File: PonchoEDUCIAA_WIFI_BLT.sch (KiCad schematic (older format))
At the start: 24 parts, among them J1 UART, SW1 Reset, SW2 Boot, U1 ESP32-WROOM

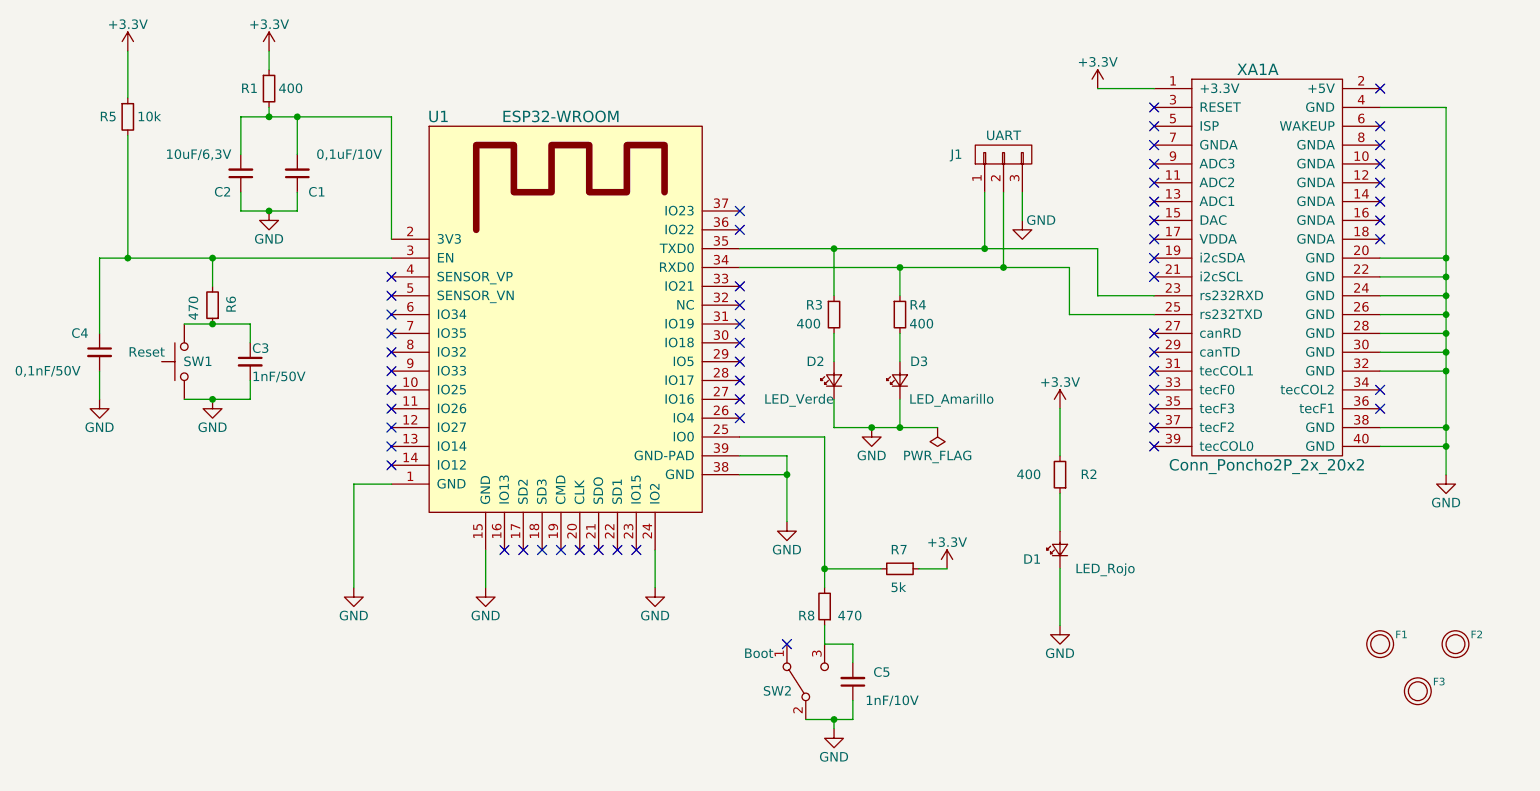
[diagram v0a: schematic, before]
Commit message: Se cargan todos los campos de los componentes del esquematico y se exporta el bom y se generan documentos
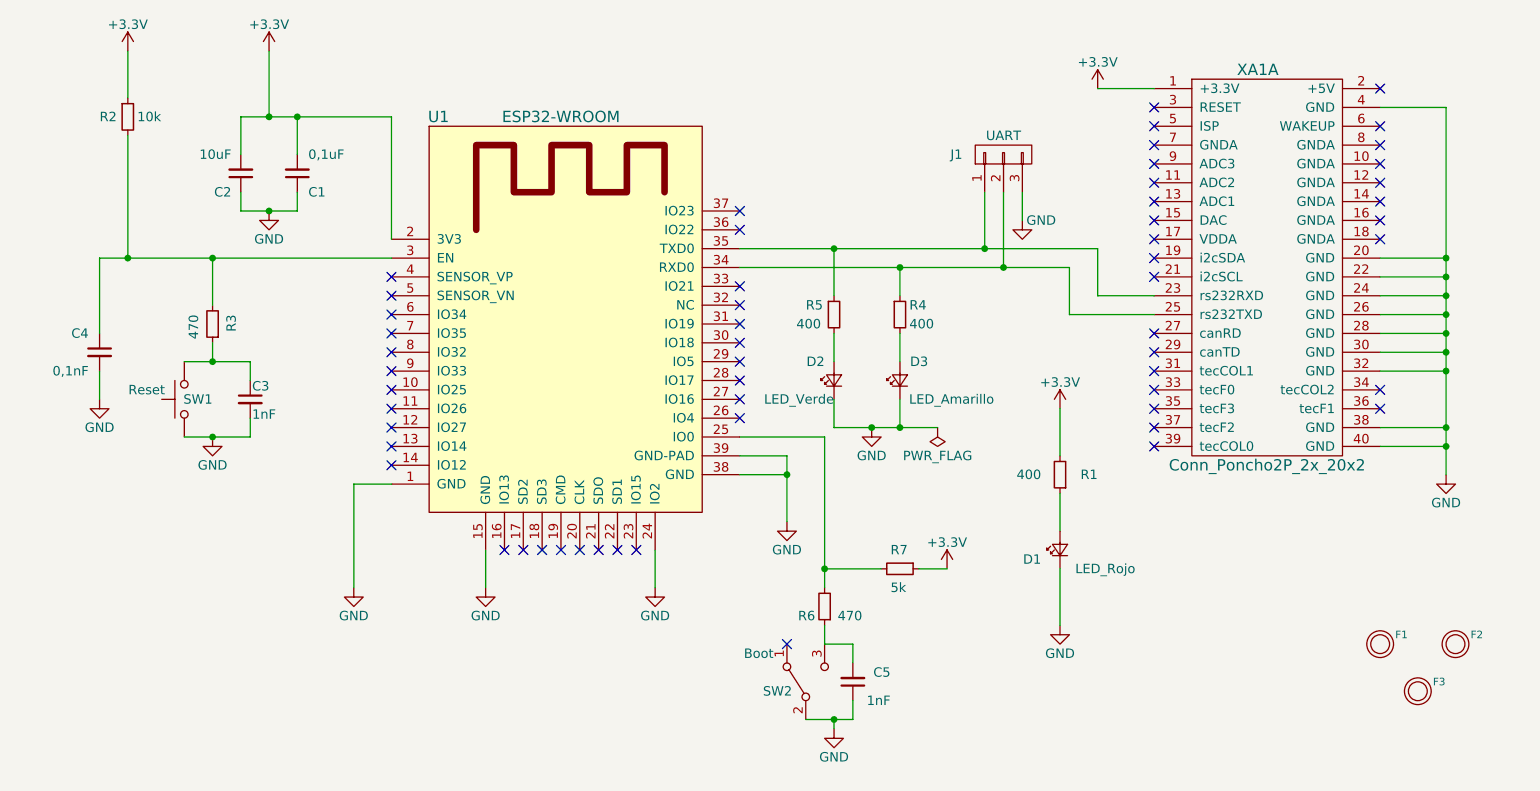
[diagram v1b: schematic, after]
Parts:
- removed R1: 400, Resistors_SMD:R_1206_HandSoldering, symbol R_Small
- C1: value 0,1uF/10V -> 0,1uF
- C2: value 10uF/6,3V -> 10uF
- C3: value 1nF/50V -> 1nF
- C4: value 0,1nF/50V -> 0,1nF
- C5: value 1nF/10V -> 1nF
- D1: Desc (none) -> LED 5MM 5V VERTICAL RED PC MNT; Digikey# (none) -> 350-1608-ND; Manf (none) -> Dialight; Manf# (none) -> 5500504F
- D2: Desc (none) -> LED 5MM VERT HE DIFF GRN PC MNT; Digikey# (none) -> 350-2814-ND; Manf (none) -> Dialight; Manf# (none) -> 5612201050F
- D3: Desc (none) -> LED 5MM 5V VERTICAL YELLOW PCMNT; Digikey# (none) -> 350-1615-ND; Manf (none) -> Dialight; Manf# (none) -> 5500804F
- J1: Desc (none) -> CONN HEADER 3POS .100 VERT TIN; Digikey# (none) -> WM4112-ND; Manf (none) -> Molex, LLC; Manf# (none) -> 0022272031
- R1: renamed from R2; Desc (none) -> RES SMD 400 OHM 0.1% 0.15W 0603; Digikey# (none) -> PAT400ACT-ND; Manf (none) -> Vishay Thin Film; Manf# (none) -> PAT0603E4000BST1
- R3: renamed from R6; Desc (none) -> RES SMD 470 OHM 1% 1/16W 0402; Digikey# (none) -> RMCF0402FT470RCT-ND; Manf (none) -> Stackpole Electronics Inc.; Manf# (none) -> RMCF0402FT470R
- R4: Desc (none) -> RES SMD 400 OHM 0.1% 0.15W 0603; Digikey# (none) -> PAT400ACT-ND; Manf (none) -> Vishay Thin Film; Manf# (none) -> PAT0603E4000BST1
- R5: renamed from R3; Desc (none) -> RES SMD 400 OHM 0.1% 0.15W 0603; Digikey# (none) -> PAT400ACT-ND; Manf (none) -> Vishay Thin Film; Manf# (none) -> PAT0603E4000BST1
- R6: renamed from R8; Desc (none) -> RES SMD 470 OHM 1% 1/16W 0402; Digikey# (none) -> RMCF0402FT470RCT-ND; Manf (none) -> Stackpole Electronics Inc.; Manf# (none) -> RMCF0402FT470R
- R7: Desc (none) -> RES SMD 5K OHM 0.05% 1/4W 1206; Digikey# (none) -> 541-3307-1-ND; Manf (none) -> Vishay Dale; Manf# (none) -> TNPU12065K00AZEN00
- SW1: Desc (none) -> SWITCH PUSH SPST-NO 0.1A 32V; Digikey# (none) -> 401-1969-ND; Manf (none) -> C&K; Manf# (none) -> D6C90 F1 LFS
- SW2: Desc (none) -> SWITCH SLIDE DPDT 300MA 6V; Digikey# (none) -> 401-2001-ND; Manf (none) -> C&K; Manf# (none) -> JS202011CQN
- U1: Desc (none) -> TXRX MOD BLE WIFI ESP-WROOM-32; Digikey# (none) -> 1528-1801-ND; Manf (none) -> Adafruit Industries LLC; Manf# (none) -> 3320
- XA1: Desc (none) -> CONN HDR 1.27MM VERT AU 20POS; Digikey# (none) -> 952-1386-ND; Manf (none) -> Harwin Inc.; Manf# (none) -> M50-3501042
- renumbered R5 to R2
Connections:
- net +3V3: now also C1.2, C2.2, U1.2 (3V3)
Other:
- moved on the sheet: C3, R3, SW1

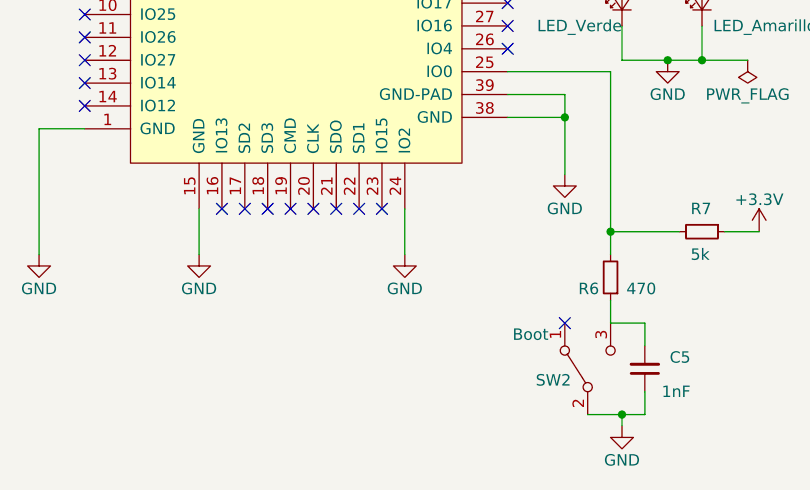
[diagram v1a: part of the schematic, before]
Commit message: Se agrega resistencia sugerida por revisor
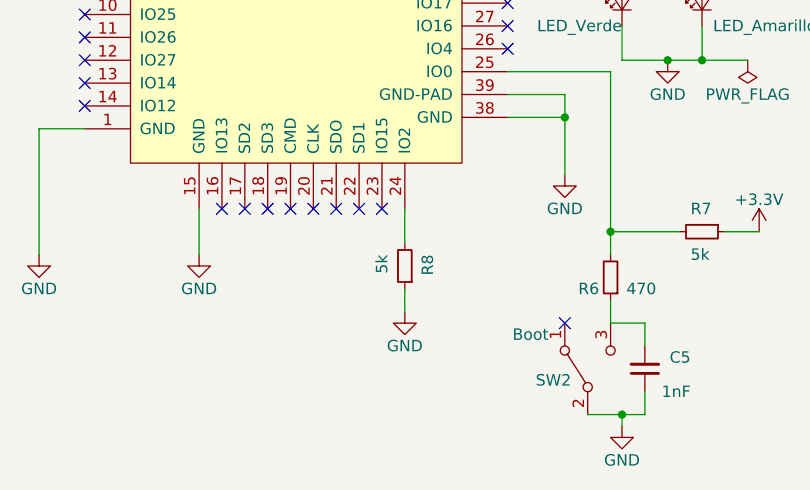
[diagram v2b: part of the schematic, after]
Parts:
- added R8: 5k, Resistors_SMD:R_1206_HandSoldering, symbol R_Small
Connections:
- net GND: now also R8.1; no longer U1.24 (IO2)
- new net: R8.2, U1.24 (IO2)
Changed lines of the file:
@@
 L GND #PWR015
 U 1 1 592E9A6D
-P 5350 5250
-F 0 "#PWR015" H 5350 5000 50  0001 C CNN
-F 1 "GND" H 5350 5100 50  0000 C CNN
-F 2 "" H 5350 5250 50  0001 C CNN
-F 3 "" H 5350 5250 50  0001 C CNN
-	1    5350 5250
+P 5350 5500
+F 0 "#PWR015" H 5350 5250 50  0001 C CNN
+F 1 "GND" H 5350 5350 50  0000 C CNN
+F 2 "" H 5350 5500 50  0001 C CNN
+F 3 "" H 5350 5500 50  0001 C CNN
+	1    5350 5500
 	1    0    0    -1
 $EndComp
@@
 Wire Wire Line
 	4450 5050 4450 5250
-Wire Wire Line
-	5350 5050 5350 5250
 Wire Wire Line
 	6300 3450 6300 3700
@@
 Wire Wire Line
 	3000 3950 3000 4050
+$Comp
+L R_Small R8
+U 1 1 594ED4F2
+P 5350 5300
+F 0 "R8" V 5250 5250 50  0000 L CNN
+F 1 "5k" V 5450 5250 50  0000 L CNN
+F 2 "Resistors_SMD:R_1206_HandSoldering" H 5350 5300 50  0001 C CNN
+F 3 "http://www.vishay.com/docs/28779/tnpue3.pdf" H 5350 5300 50  0001 C CNN
+F 4 "Vishay Dale" H 5350 5300 60  0001 C CNN "Manf"
+F 5 "TNPU12065K00AZEN00" H 5350 5300 60  0001 C CNN "Manf#"
+F 6 "541-3307-1-ND" H 5350 5300 60  0001 C CNN "Digikey#"
+F 7 "RES SMD 5K OHM 0.05% 1/4W 1206" H 5350 5300 60  0001 C CNN "Desc"
+	1    5350 5300
+	-1   0    0    1
+$EndComp
+Wire Wire Line
+	5350 5050 5350 5200
+Wire Wire Line
+	5350 5400 5350 5500
 $EndSCHEMATC

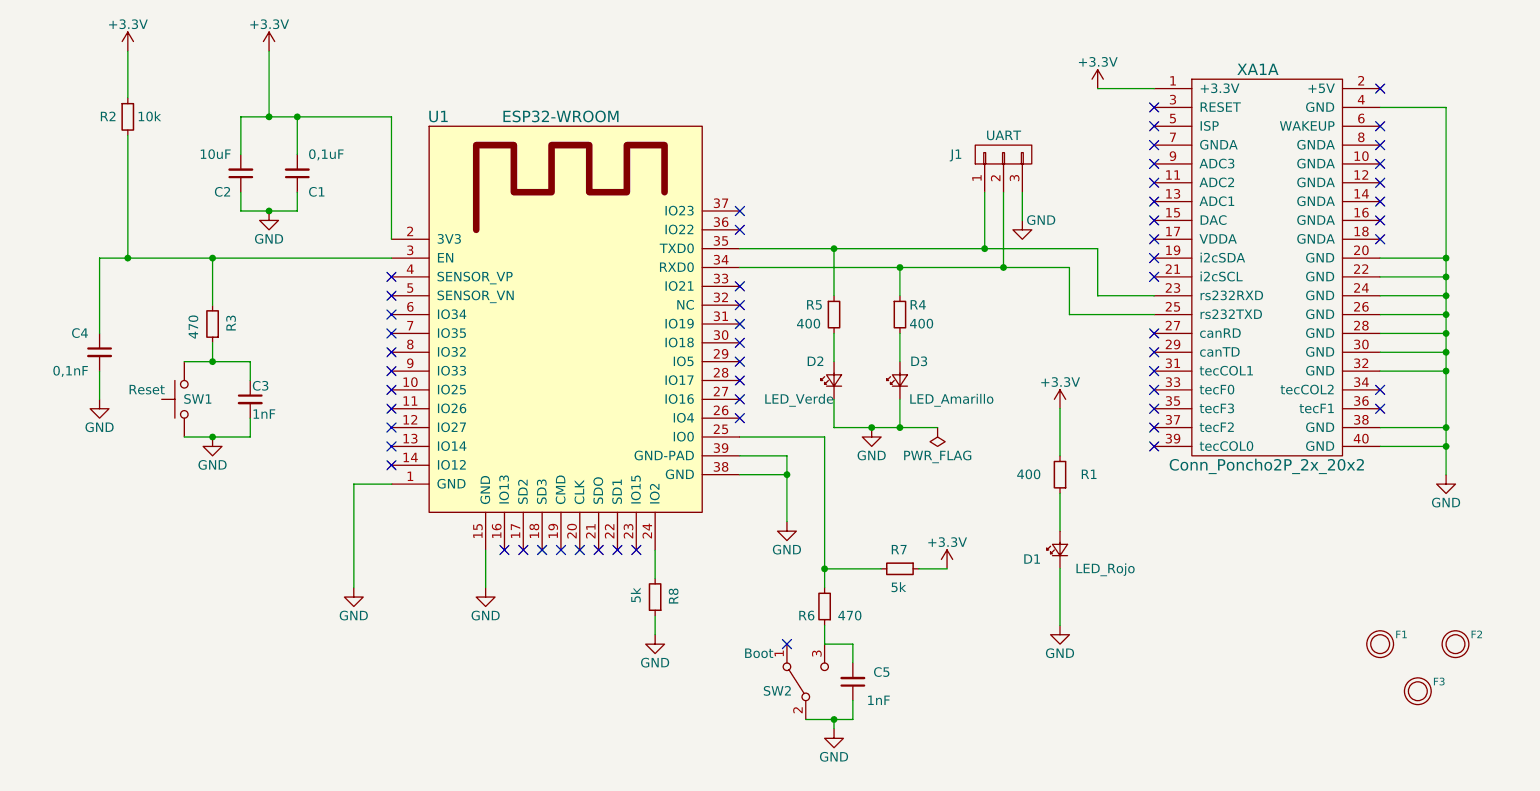
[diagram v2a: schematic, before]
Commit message: Se realizan cambios sugeridos por revisor Diego Bregni: rotulos, unificar resistencias 805, mejora prolijidad de conexiones, se agrega codigo mouser, revisiones y proyecto en carpeta doc.
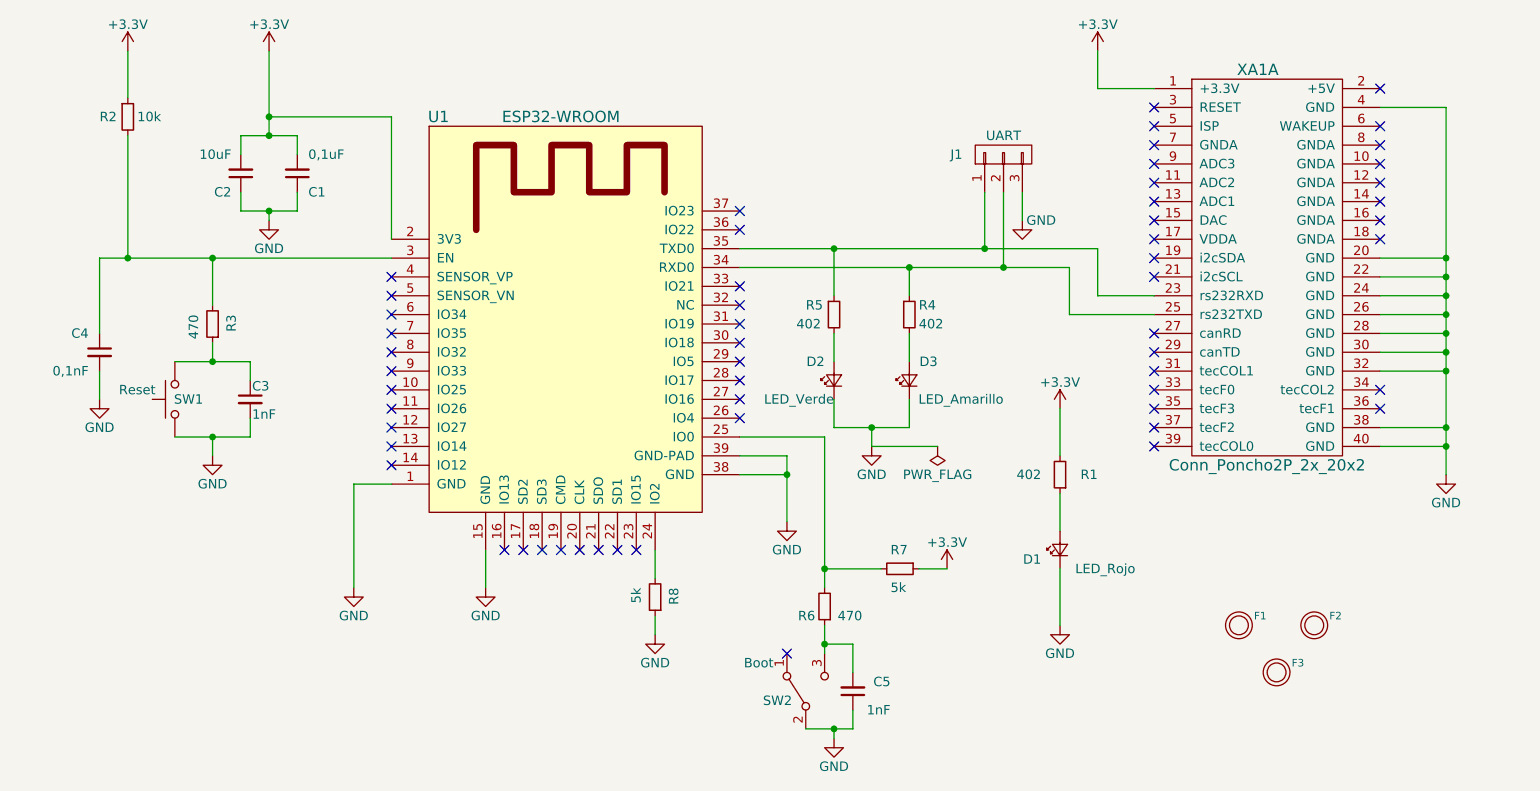
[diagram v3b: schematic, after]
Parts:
- C1: Mouser# (none) -> 581-02016D104KAT2A
- C2: Mouser# (none) -> 81-GRM219R60J106KE9D
- C3: Mouser# (none) -> 81-GRM1555C1H101JA1D
- C4: Mouser# (none) -> 81-GRM1555C1H100JA1D
- C5: Mouser# (none) -> 581-0201ZA101JAT2A
- D1: Mouser# (none) -> 645-550-0504F
- D2: Mouser# (none) -> 645-561-2201-050F
- D3: Mouser# (none) -> 645-550-0804F
- J1: Mouser# (none) -> 538-22-27-2031
- R1, R4, R5: value 400 -> 402; footprint Resistors_SMD:R_1206_HandSoldering -> Resistors_SMD:R_0805_HandSoldering; Desc RES SMD 400 OHM 0.1% 0.15W 0603 -> RES SMD 402 OHM 1% 1/8W 0805; Digikey# PAT400ACT-ND -> 311-402CRCT-ND; Manf Vishay Thin Film -> Yageo; Manf# PAT0603E4000BST1 -> RC0805FR-07402RL; Mouser# (none) -> 603-RC0805FR-07402RL
- R2: footprint Resistors_SMD:R_1206_HandSoldering -> Resistors_SMD:R_0805_HandSoldering; Desc 10k Ohm ±0.1% 0.063W, 1/16W Chip Resistor 0402 (1005 Metric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 -> RES SMD 10K OHM 0.1% 1/8W 0805; Digikey# A102579CT-ND -> P10KDACT-ND; Manf TE Connectivity Passive Product -> Panasonic Electronic Components; Manf# CPF0402B10KE1 -> ERA-6AEB103V; Mouser# (none) -> 667-ERA-6AEB103V
- R3, R6: footprint Resistors_SMD:R_1206_HandSoldering -> Resistors_SMD:R_0805_HandSoldering; Desc RES SMD 470 OHM 1% 1/16W 0402 -> RES SMD 470 OHM 1% 1/8W 0805; Digikey# RMCF0402FT470RCT-ND -> 311-470CRCT-ND; Manf Stackpole Electronics Inc. -> Yageo; Manf# RMCF0402FT470R -> RC0805FR-07470RL; Mouser# (none) -> 603-RC0805FR-07470RL
- R7, R8: footprint Resistors_SMD:R_1206_HandSoldering -> Resistors_SMD:R_0805_HandSoldering; Desc RES SMD 5K OHM 0.05% 1/4W 1206 -> RES SMD 5K OHM 1% 1/8W 0805; Digikey# 541-3307-1-ND -> CRCW08055K00FKTA-ND; Manf# TNPU12065K00AZEN00 -> CRCW08055K00FKTA; Mouser# (none) -> 71-CRCW0805-5K
- SW1: Mouser# (none) -> 611-D6C90F1LFS
- SW2: Mouser# (none) -> 611-JS202011CQN
- U1: Mouser# (none) -> 485-3320
- XA1: Mouser# (none) -> 855-M50-3501042
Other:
- moved on the sheet: C5, D3, F1, F2, F3, R4, SW1, SW2

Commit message: Primer ruteo tentativo
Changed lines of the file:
@@
 L PWR_FLAG #FLG013
 U 1 1 59279118
-P 6850 4500
-F 0 "#FLG013" H 6850 4575 50  0001 C CNN
-F 1 "PWR_FLAG" H 6850 4650 50  0000 C CNN
-F 2 "" H 6850 4500 50  0001 C CNN
-F 3 "" H 6850 4500 50  0001 C CNN
-	1    6850 4500
+P 9750 4500
+F 0 "#FLG013" H 9750 4575 50  0001 C CNN
+F 1 "PWR_FLAG" H 9750 4650 50  0000 C CNN
+F 2 "" H 9750 4500 50  0001 C CNN
+F 3 "" H 9750 4500 50  0001 C CNN
+	1    9750 4500
 	-1   0    0    1
 $EndComp
@@
 Connection ~ 9550 4400
 Wire Wire Line
-	9200 4500 9550 4500
+	9200 4500 9750 4500
 Connection ~ 9550 4500
 Connection ~ 6700 3550
@@
 	6500 4400 6500 4500
 Wire Wire Line
-	6500 4500 6850 4500
-Wire Wire Line
 	3000 4550 3000 4450
